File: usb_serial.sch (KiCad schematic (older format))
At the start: 2 parts, among them U9 HT42B534

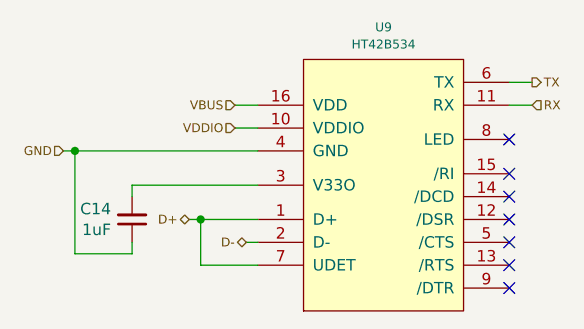
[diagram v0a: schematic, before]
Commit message: clear existing annotations from schematic
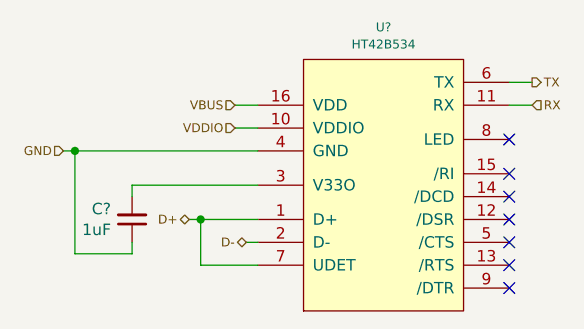
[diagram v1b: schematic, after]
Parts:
- renumbered C14 to C?, U9 to U?
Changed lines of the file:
@@
 $EndDescr
 $Comp
-L phone:HT42B534 U9
+L phone:HT42B534 U?
 U 1 1 5C941C5F
 P 3400 2550
-F 0 "U9" H 3400 3241 39  0000 C CNN
+F 0 "U?" H 3400 3241 39  0000 C CNN
 F 1 "HT42B534" H 3400 3166 39  0000 C CNN
 F 2 "Package_SO:SOIC-16_3.9x9.9mm_P1.27mm" H 3400 2600 39  0001 C CNN
@@
 GND
 $Comp
-L Device:C_Small C14
+L Device:C_Small C?
 U 1 1 5C942CE1
 P 2300 2700
-F 0 "C14" H 2208 2654 50  0000 R CNN
+F 0 "C?" H 2208 2654 50  0000 R CNN
 F 1 "1uF" H 2208 2745 50  0000 R CNN
 F 2 "Capacitor_SMD:C_0603_1608Metric_Pad1.05x0.95mm_HandSolder" H 2300 2700 50  0001 C CNN

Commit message: annotate schematic and tweak some footprint associations
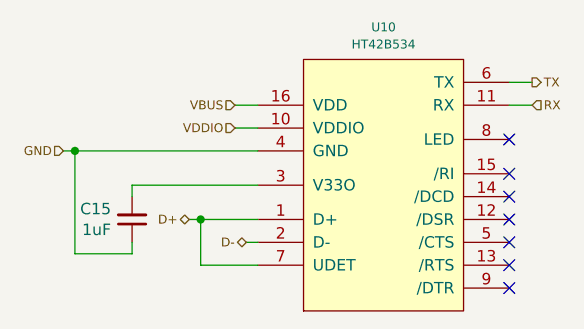
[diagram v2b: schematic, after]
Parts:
- gave numbers to parts that had none: 2
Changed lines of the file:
@@
 $EndDescr
 $Comp
-L phone:HT42B534 U?
+L phone:HT42B534 U10
 U 1 1 5C941C5F
 P 3400 2550
-F 0 "U?" H 3400 3241 39  0000 C CNN
+F 0 "U10" H 3400 3241 39  0000 C CNN
 F 1 "HT42B534" H 3400 3166 39  0000 C CNN
 F 2 "Package_SO:SOIC-16_3.9x9.9mm_P1.27mm" H 3400 2600 39  0001 C CNN
@@
 GND
 $Comp
-L Device:C_Small C?
+L Device:C_Small C15
 U 1 1 5C942CE1
 P 2300 2700
-F 0 "C?" H 2208 2654 50  0000 R CNN
+F 0 "C15" H 2208 2654 50  0000 R CNN
 F 1 "1uF" H 2208 2745 50  0000 R CNN
 F 2 "Capacitor_SMD:C_0603_1608Metric_Pad1.05x0.95mm_HandSolder" H 2300 2700 50  0001 C CNN
